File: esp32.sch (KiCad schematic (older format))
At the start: 41 parts, among them J1 Micro_SD_Card, J10 Conn_01x01, J11 Conn_01x04, J12 Conn_01x01, J13 Conn_01x01, J14 Conn_01x01, J15 Conn_01x01, J18 Conn_01x02, J2 Conn_01x06, J25 Conn_01x01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

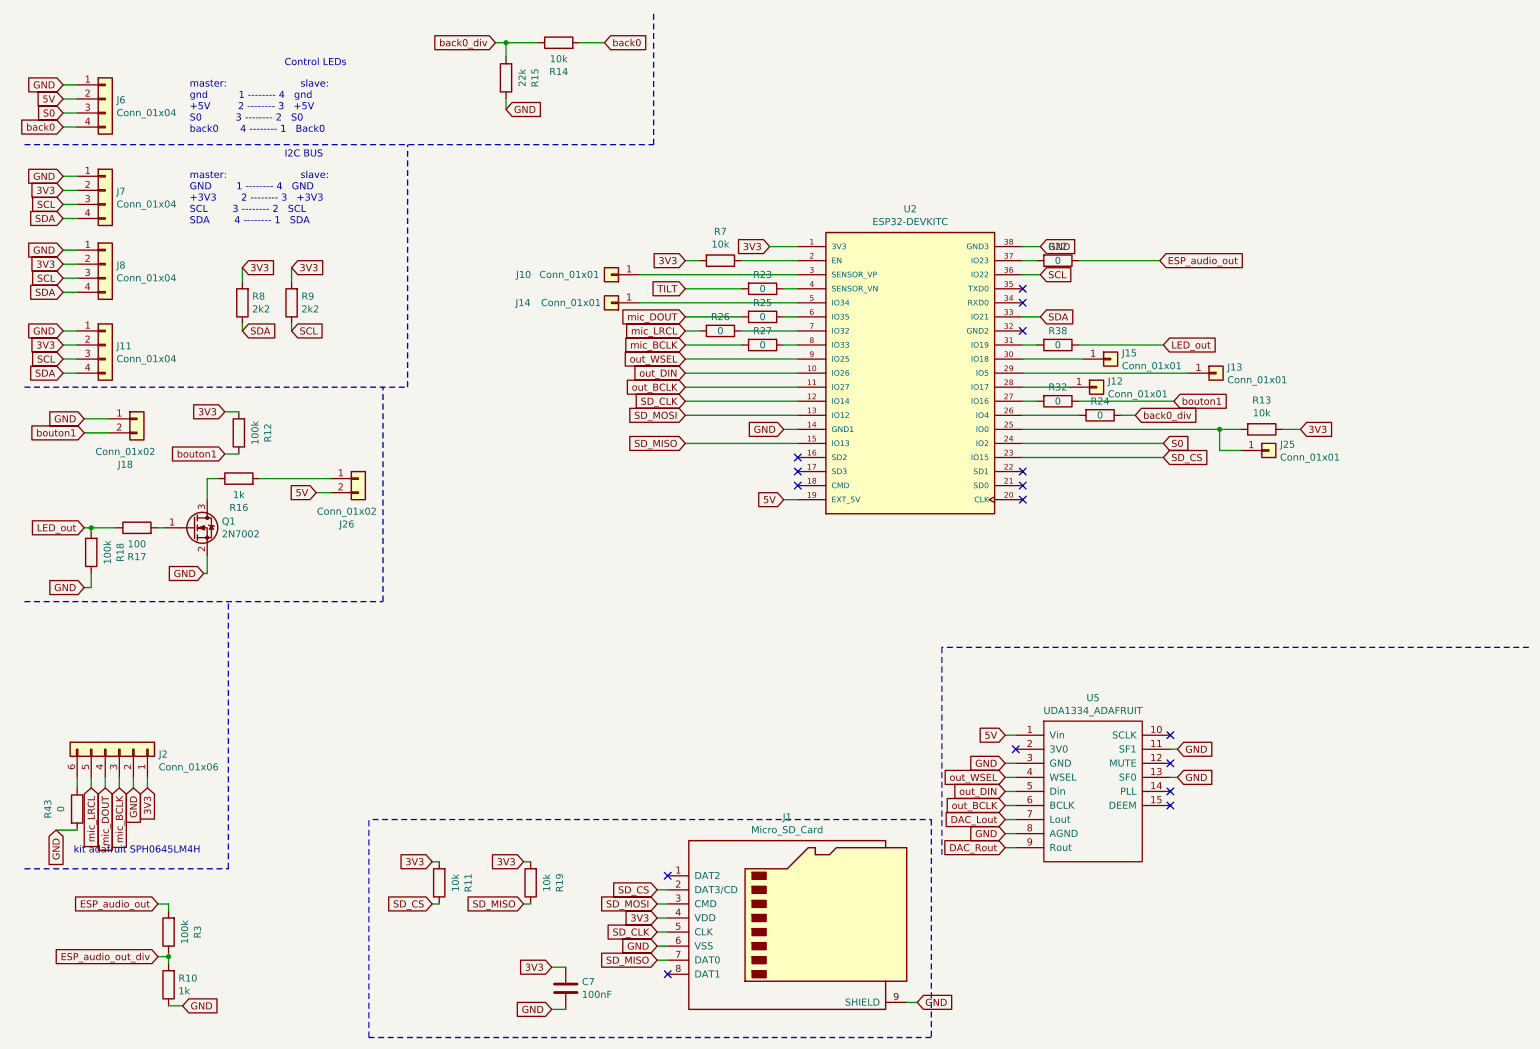
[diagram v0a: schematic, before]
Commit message: ajout spi + placement + routage
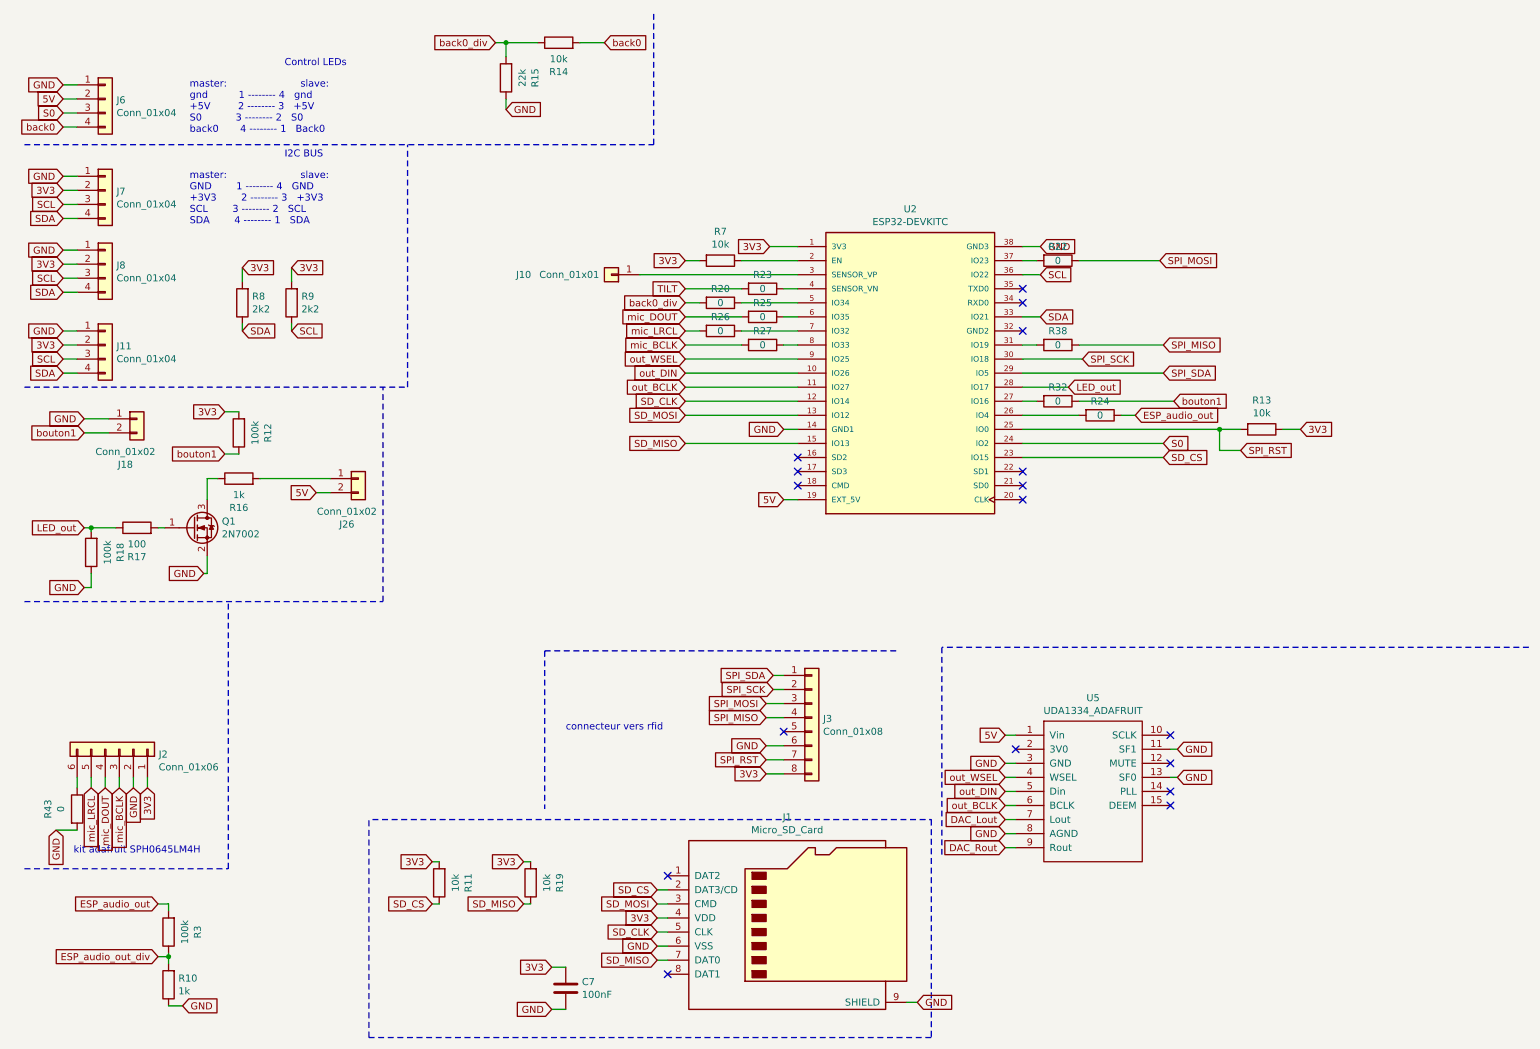
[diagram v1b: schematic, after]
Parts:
- removed J12, J13, J14, J15, J25: Conn_01x01, Connector_PinHeader_2.54mm:PinHeader_1x01_P2.54mm_Vertical, symbol Connector_Generic:Conn_01x01
- added J3: Conn_01x08, Connector_PinSocket_2.54mm:PinSocket_1x08_P2.54mm_Vertical, symbol Connector_Generic:Conn_01x08
- added R20: 0, Resistor_SMD:R_0603_1608Metric_Pad1.05x0.95mm_HandSolder, symbol Device:R
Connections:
- net 3V3: now also J3.8 (Pin_8)
- net ESP_audio_out: now also R24.1; no longer R22.1
- net GND: now also J3.6 (Pin_6)
- net LED_out: now also U2.28 (IO17); no longer R38.1
- net back0_div: now also R20.2; no longer R24.1
- net SPI_RST: now reaches R13.2, U2.25 (IO0)
- net SPI_RST: now also J3.7 (Pin_7)
- net SPI_SDA: now reaches U2.29 (IO5)
- net SPI_SDA: now also J3.1 (Pin_1)
- net SPI_SCK: now reaches U2.30 (IO18)
- net SPI_SCK: now also J3.2 (Pin_2)
- net at U2.5 (IO34): now also R20.1
- new net SPI_MISO: J3.4 (Pin_4), R38.1
- new net SPI_MOSI: J3.3 (Pin_3), R22.1
- no-connect marks 16 -> 17
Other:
- note added: "connecteur vers rfid"
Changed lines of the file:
@@
 Wire Wire Line
 	775  3050 875  3050
-Text GLabel 8575 2250 2    50   Input ~ 0
+Text GLabel 8400 3350 2    50   Input ~ 0
 ESP_audio_out
 $Comp
@@
 Wire Wire Line
 	925  3475 1100 3475
-Text GLabel 8600 2850 2    50   Input ~ 0
+Text GLabel 7925 3150 2    50   Input ~ 0
 LED_out
 Text GLabel 925  4150 0    50   Input ~ 0
@@
 Wire Wire Line
 	7600 3450 9000 3450
-$Comp
-L Connector_Generic:Conn_01x01 J25
-U 1 1 5FE1105E
-P 9350 3600
-F 0 "J25" H 9430 3642 50  0000 L CNN
-F 1 "Conn_01x01" H 9430 3551 50  0000 L CNN
-F 2 "Connector_PinHeader_2.54mm:PinHeader_1x01_P2.54mm_Vertical" H 9350 3600 50  0001 C CNN
-F 3 "~" H 9350 3600 50  0001 C CNN
-	1    9350 3600
-	1    0    0    -1
-$EndComp
 Wire Wire Line
 	9150 3600 9000 3600
@@
 	3850 700  3925 700
 Connection ~ 3925 700
-Text GLabel 8400 3350 2    50   Input ~ 0
+Text GLabel 5200 2550 0    50   Input ~ 0
 back0_div
 Text GLabel 5200 3550 0    50   Input ~ 0
@@
 Wire Wire Line
 	7600 3550 8600 3550
-$Comp
-L Connector_Generic:Conn_01x01 J12
-U 1 1 603B0996
-P 8125 3150
-F 0 "J12" H 8205 3192 50  0000 L CNN
-F 1 "Conn_01x01" H 8205 3101 50  0000 L CNN
-F 2 "Connector_PinHeader_2.54mm:PinHeader_1x01_P2.54mm_Vertical" H 8125 3150 50  0001 C CNN
-F 3 "~" H 8125 3150 50  0001 C CNN
-	1    8125 3150
-	1    0    0    -1
-$EndComp
-$Comp
-L Connector_Generic:Conn_01x01 J13
-U 1 1 603B18E4
-P 8975 3050
-F 0 "J13" H 9055 3092 50  0000 L CNN
-F 1 "Conn_01x01" H 9055 3001 50  0000 L CNN
-F 2 "Connector_PinHeader_2.54mm:PinHeader_1x01_P2.54mm_Vertical" H 8975 3050 50  0001 C CNN
-F 3 "~" H 8975 3050 50  0001 C CNN
-	1    8975 3050
-	1    0    0    -1
-$EndComp
 Wire Wire Line
 	7925 3150 7600 3150
 Text GLabel 8675 3250 2    50   Input ~ 0
 bouton1
-$Comp
-L Connector_Generic:Conn_01x01 J14
-U 1 1 603BD4F7
-P 4675 2550
-F 0 "J14" H 5250 2550 50  0000 L CNN
-F 1 "Conn_01x01" H 4750 2550 50  0000 L CNN
-F 2 "Connector_PinHeader_2.54mm:PinHeader_1x01_P2.54mm_Vertical" H 4675 2550 50  0001 C CNN
-F 3 "~" H 4675 2550 50  0001 C CNN
-	1    4675 2550
-	-1   0    0    1
-$EndComp
-$Comp
-L Connector_Generic:Conn_01x01 J15
-U 1 1 603BD71F
-P 8225 2950
-F 0 "J15" H 8305 2992 50  0000 L CNN
-F 1 "Conn_01x01" H 8305 2901 50  0000 L CNN
-F 2 "Connector_PinHeader_2.54mm:PinHeader_1x01_P2.54mm_Vertical" H 8225 2950 50  0001 C CNN
-F 3 "~" H 8225 2950 50  0001 C CNN
-	1    8225 2950
-	1    0    0    -1
-$EndComp
 Wire Wire Line
 	7600 2950 8025 2950
@@
 	8300 3350 8400 3350
 Wire Wire Line
-	4875 2550 6000 2550
-Wire Wire Line
 	7600 3250 7700 3250
 Wire Wire Line
 	8000 3250 8675 3250
 Wire Wire Line
-	7600 3050 8775 3050
-Wire Wire Line
 	5200 3250 6000 3250
 Wire Wire Line
@@
 Wire Notes Line
 	7025 5000 7025 6475
+$Comp
+L Connector_Generic:Conn_01x08 J3
+U 1 1 606CE771
+P 6100 5500
+F 0 "J3" H 6180 5492 50  0000 L CNN
+F 1 "Conn_01x08" H 6180 5401 50  0000 L CNN
+F 2 "Connector_PinSocket_2.54mm:PinSocket_1x08_P2.54mm_Vertical" H 6100 5500 50  0001 C CNN
+F 3 "~" H 6100 5500 50  0001 C CNN
+	1    6100 5500
+	1    0    0    -1
+$EndComp
+Text GLabel 5825 5200 0    50   Input ~ 0
+SPI_SDA
+Text GLabel 5825 5300 0    50   Input ~ 0
+SPI_SCK
+Text GLabel 5775 5400 0    50   Input ~ 0
+SPI_MOSI
+Text GLabel 5775 5500 0    50   Input ~ 0
+SPI_MISO
+NoConn ~ 5900 5600
+Text GLabel 5775 5700 0    50   Input ~ 0
+GND
+Text GLabel 5775 5900 0    50   Input ~ 0
+3V3
+Text GLabel 5775 5800 0    50   Input ~ 0
+SPI_RST
+Wire Wire Line
+	5825 5200 5900 5200
+Wire Wire Line
+	5825 5300 5900 5300
+Wire Wire Line
+	5775 5400 5900 5400
+Wire Wire Line
+	5775 5500 5900 5500
+Wire Wire Line
+	5775 5700 5900 5700
+Wire Wire Line
+	5775 5800 5900 5800
+Wire Wire Line
+	5775 5900 5900 5900
+Text Notes 4350 5600 0    50   ~ 0
+connecteur vers rfid
+Wire Notes Line
+	6700 5025 4200 5025
+Wire Notes Line
+	4200 5025 4200 6150
+Text GLabel 8600 3050 2    50   Input ~ 0
+SPI_SDA
+Text GLabel 8025 2950 2    50   Input ~ 0
+SPI_SCK
+Text GLabel 8575 2250 2    50   Input ~ 0
+SPI_MOSI
+Text GLabel 8600 2850 2    50   Input ~ 0
+SPI_MISO
+Text GLabel 9150 3600 2    50   Input ~ 0
+SPI_RST
+Wire Wire Line
+	7600 3050 8600 3050
+$Comp
+L Device:R R20
+U 1 1 60720E58
+P 5450 2550
+F 0 "R20" V 5350 2550 50  0000 C CNN
+F 1 "0" V 5450 2550 50  0000 C CNN
+F 2 "Resistor_SMD:R_0603_1608Metric_Pad1.05x0.95mm_HandSolder" V 5380 2550 50  0001 C CNN
+F 3 "~" H 5450 2550 50  0001 C CNN
+	1    5450 2550
+	0    1    1    0
+$EndComp
+Wire Wire Line
+	5600 2550 6000 2550
+Wire Wire Line
+	5200 2550 5300 2550
 $EndSCHEMATC

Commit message: correction pcb
ajout infos sur silk
changement connecteur jst xh 4 points pour un coudé.
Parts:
- J6: footprint Connector_JST:JST_XH_B4B-XH-A_1x04_P2.50mm_Vertical -> Connector_JST:JST_XH_S4B-XH-A_1x04_P2.50mm_Horizontal
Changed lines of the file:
@@
 F 0 "J6" H 1155 1092 50  0000 L CNN
 F 1 "Conn_01x04" H 1155 1001 50  0000 L CNN
-F 2 "Connector_JST:JST_XH_B4B-XH-A_1x04_P2.50mm_Vertical" H 1075 1100 50  0001 C CNN
+F 2 "Connector_JST:JST_XH_S4B-XH-A_1x04_P2.50mm_Horizontal" H 1075 1100 50  0001 C CNN
 F 3 "~" H 1075 1100 50  0001 C CNN
 	1    1075 1100

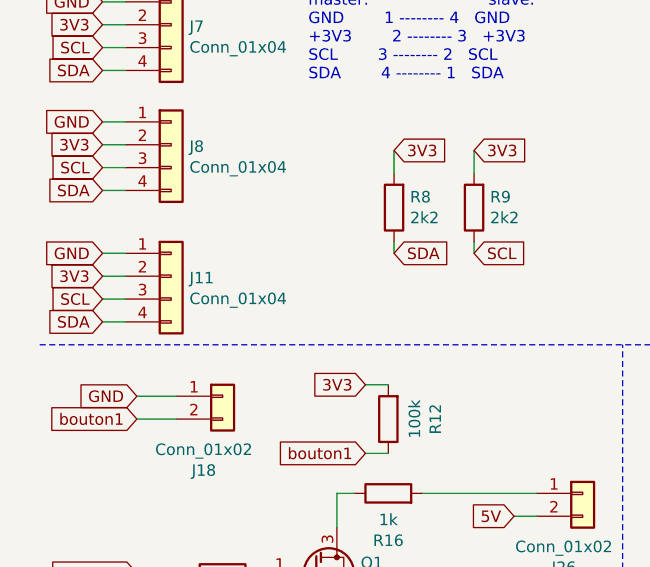
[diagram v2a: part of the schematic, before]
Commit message: ajout strap sur dernier connecteur I2C
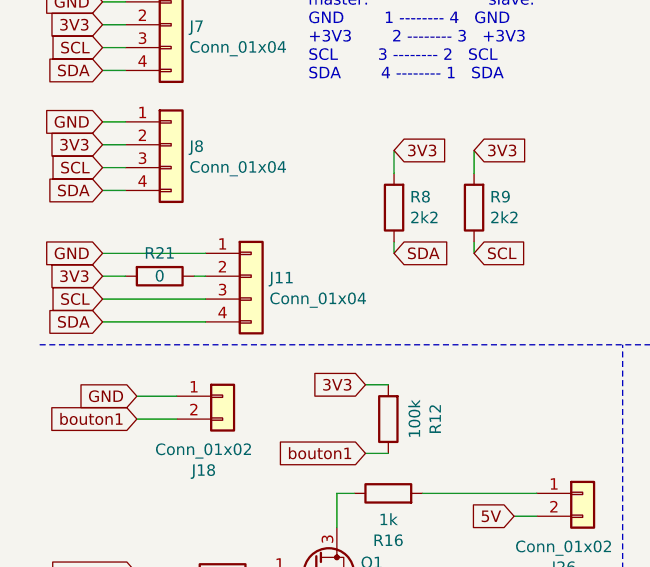
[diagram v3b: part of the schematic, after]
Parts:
- added R21: 0, Resistor_SMD:R_0603_1608Metric_Pad1.05x0.95mm_HandSolder, symbol Device:R
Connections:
- net 3V3: now also R21.2; no longer J11.2 (Pin_2)
- new net: J11.2 (Pin_2), R21.1
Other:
- moved on the sheet: J11
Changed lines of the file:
@@
 L Connector_Generic:Conn_01x04 J?
 U 1 1 5FE053D1
-P 1075 2850
+P 1425 2850
 AR Path="/5FC6D1B4/5FDF95DF/5FE053D1" Ref="J?"  Part="1"
 AR Path="/5FC6D1B4/5FE053D1" Ref="J11"  Part="1"
-F 0 "J11" H 1155 2842 50  0000 L CNN
-F 1 "Conn_01x04" H 1155 2751 50  0000 L CNN
-F 2 "Connector_JST:JST_XH_B4B-XH-A_1x04_P2.50mm_Vertical" H 1075 2850 50  0001 C CNN
-F 3 "~" H 1075 2850 50  0001 C CNN
-	1    1075 2850
+F 0 "J11" H 1505 2842 50  0000 L CNN
+F 1 "Conn_01x04" H 1505 2751 50  0000 L CNN
+F 2 "Connector_JST:JST_XH_B4B-XH-A_1x04_P2.50mm_Vertical" H 1425 2850 50  0001 C CNN
+F 3 "~" H 1425 2850 50  0001 C CNN
+	1    1425 2850
 	1    0    0    -1
 $EndComp
@@
 SDA
 Wire Wire Line
-	775  2750 875  2750
-Wire Wire Line
 	775  2850 875  2850
 Text GLabel 775  2750 0    50   Input ~ 0
 GND
-Wire Wire Line
-	775  2950 875  2950
-Wire Wire Line
-	775  3050 875  3050
 Text GLabel 8400 3350 2    50   Input ~ 0
 ESP_audio_out
@@
 Wire Wire Line
 	5200 2550 5300 2550
+$Comp
+L Device:R R21
+U 1 1 60706511
+P 1025 2850
+F 0 "R21" V 925 2850 50  0000 C CNN
+F 1 "0" V 1025 2850 50  0000 C CNN
+F 2 "Resistor_SMD:R_0603_1608Metric_Pad1.05x0.95mm_HandSolder" V 955 2850 50  0001 C CNN
+F 3 "~" H 1025 2850 50  0001 C CNN
+	1    1025 2850
+	0    1    1    0
+$EndComp
+Wire Wire Line
+	1225 2850 1175 2850
+Wire Wire Line
+	775  2750 1225 2750
+Wire Wire Line
+	775  3050 1225 3050
+Wire Wire Line
+	775  2950 1225 2950
 $EndSCHEMATC

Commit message: maj split librairie
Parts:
- U2: footprint Chimere:MODULE_ESP32-DEVKITC -> Chimere_comps:MODULE_ESP32-DEVKITC; symbol Chimere:ESP32-DEVKITC -> Chimere_comps:ESP32-DEVKITC
- U5: footprint Chimere:Adafruit_UDA1334 -> Chimere_comps:Adafruit_UDA1334; symbol Chimere:UDA1334_ADAFRUIT -> Chimere_comps:UDA1334_ADAFRUIT
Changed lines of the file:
@@
 $EndDescr
 $Comp
-L Chimere:ESP32-DEVKITC U2
+L Chimere_comps:ESP32-DEVKITC U2
 U 1 1 5FC6D4F6
 P 6800 3050
+AR Path="/5FC6D4F6" Ref="U2"  Part="1"
+AR Path="/5FC6D1B4/5FC6D4F6" Ref="U2"  Part="1"
 F 0 "U2" H 6800 4217 50  0000 C CNN
 F 1 "ESP32-DEVKITC" H 6800 4126 50  0000 C CNN
-F 2 "Chimere:MODULE_ESP32-DEVKITC" H 6800 3050 50  0001 L BNN
+F 2 "Chimere_comps:MODULE_ESP32-DEVKITC" H 6800 3050 50  0001 L BNN
 F 3 "" H 6800 3050 50  0001 L BNN
 F 4 "Manufacturer Recommendations" H 6800 3050 50  0001 L BNN "STANDARD"
@@
 	5200 2950 6000 2950
 $Comp
-L Chimere:UDA1334_ADAFRUIT U5
+L Chimere_comps:UDA1334_ADAFRUIT U5
 U 1 1 606CC25D
 P 8100 5925
+AR Path="/606CC25D" Ref="U5"  Part="1"
+AR Path="/5FC6D1B4/606CC25D" Ref="U5"  Part="1"
 F 0 "U5" H 8100 6490 50  0000 C CNN
 F 1 "UDA1334_ADAFRUIT" H 8100 6399 50  0000 C CNN
-F 2 "Chimere:Adafruit_UDA1334" H 7950 5925 50  0001 C CNN
+F 2 "Chimere_comps:Adafruit_UDA1334" H 7950 5925 50  0000 C CNN
 F 3 "" H 7950 5925 50  0001 C CNN
 	1    8100 5925
